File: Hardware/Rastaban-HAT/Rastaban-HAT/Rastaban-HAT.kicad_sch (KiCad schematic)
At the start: 65 parts, among them J1 1778780, J10 GPIO, J11 Conn_01x06_Male, J2 1778780, J3 1778780, J4 Screw_Terminal_01x02, J5 Jack-DC 12V+, J6 SM04B-SRSS-TB(LF)(SN), J7 Screw_Terminal_01x02, J8 Screw_Terminal_01x02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

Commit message: All files created with Jan
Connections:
- net at M1.1 (+): now also F1.2; no longer Q1.3 (D)
- net at M1.2 (-): now also Q1.3 (D); no longer F1.2
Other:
- moved on the sheet: M1
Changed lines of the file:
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@@
     (pin "2")
   )
-  (symbol (lib_id "Motor:Fan") (at 39.37 81.28 180) (unit 1)
-    (in_bom yes) (on_board yes)
-    (property "Reference" "M1" (id 0) (at 44.45 81.28 0))
-    (property "Value" "Fan" (id 1) (at 45.72 83.185 0)
-      (effects (font (size 1.27 1.27)) hide)
-    )
-    (property "Footprint" "Connector_PinHeader_2.54mm:PinHeader_1x02_P2.54mm_Vertical" (id 2) (at 39.37 81.534 0)
-      (effects (font (size 1.27 1.27)) hide)
-    )
-    (property "Datasheet" "~" (id 3) (at 39.37 81.534 0)
-      (effects (font (size 1.27 1.27)) hide)
-    )
-    (property "Purpose" "Cooling fan" (id 4) (at 48.26 84.455 0))
+  (symbol (lib_id "Motor:Fan") (at 39.37 83.82 0) (unit 1)
+    (in_bom yes) (on_board yes)
+    (property "Reference" "M1" (id 0) (at 34.29 83.82 0))
+    (property "Value" "Fan" (id 1) (at 33.02 81.915 0)
+      (effects (font (size 1.27 1.27)) hide)
+    )
+    (property "Footprint" "Connector_PinHeader_2.54mm:PinHeader_1x02_P2.54mm_Vertical" (id 2) (at 39.37 83.566 0)
+      (effects (font (size 1.27 1.27)) hide)
+    )
+    (property "Datasheet" "~" (id 3) (at 39.37 83.566 0)
+      (effects (font (size 1.27 1.27)) hide)
+    )
+    (property "Purpose" "Cooling fan" (id 4) (at 30.48 80.645 0))
     (pin "1")
     (pin "2")
@@
       (effects (font (size 1.27 1.27)) (justify right))
     )
-    (property "Value" "100uF 10V" (id 1) (at 38.735 38.735 0)
+    (property "Value" "100uF 10V" (id 1) (at 37.465 38.735 0)
       (effects (font (size 1.27 1.27)) (justify right))
     )
@@
       (effects (font (size 1.27 1.27)) (justify left))
     )
-    (property "Value" "10uF 10V" (id 1) (at 20.32 38.735 0)
-      (effects (font (size 1.27 1.27)) (justify left))
-    )
+    (property "Value" "10uF 10V" (id 1) (at 19.685 38.735 0)
+      (effects (font (size 1.27 1.27)) (justify left))
+    )

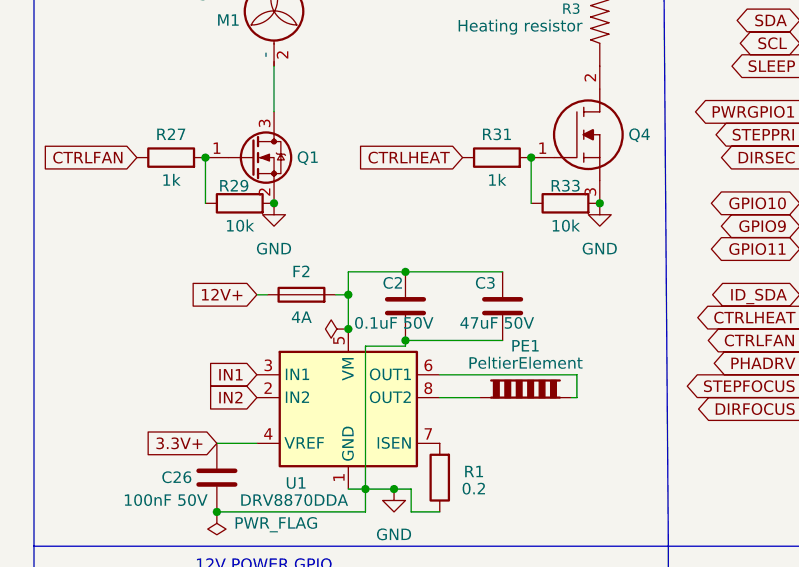
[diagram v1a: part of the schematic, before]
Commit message: enh pcb component layout
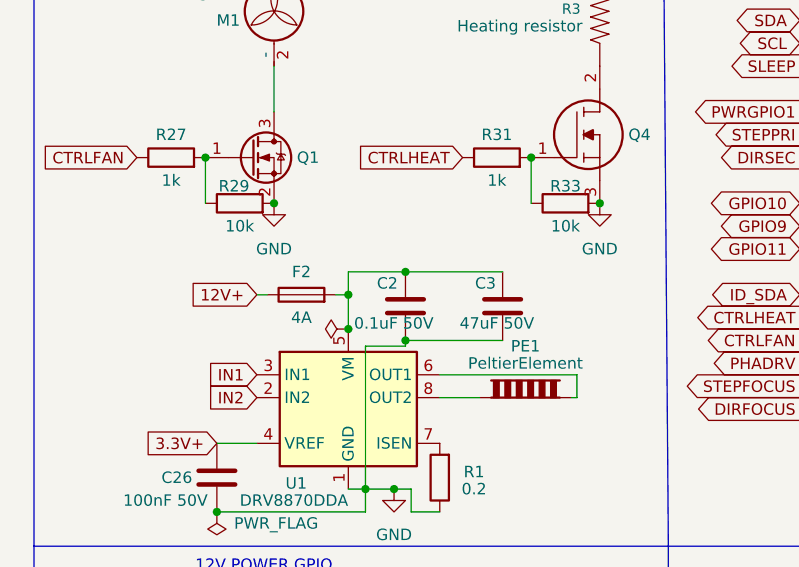
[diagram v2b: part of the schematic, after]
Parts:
- C1, C2, C20, C21, C25, C26, C3, C4: Purpose (none) -> decoupling
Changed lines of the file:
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@@
+      (effects (font (size 1.27 1.27)) hide)
+    )
+    (property "Purpose" "decoupling" (id 7) (at 64.77 115.57 0)
       (effects (font (size 1.27 1.27)) hide)
     )
@@
       (effects (font (size 1.27 1.27)) hide)
     )
+    (property "Purpose" "decoupling" (id 5) (at 198.12 71.755 0)
+      (effects (font (size 1.27 1.27)) hide)
+    )
     (pin "1")
     (pin "2")
@@
       (effects (font (size 1.27 1.27)) hide)
     )
+    (property "Purpose" "decoupling" (id 5) (at 196.85 117.475 0)
+      (effects (font (size 1.27 1.27)) hide)
+    )
     (pin "1")
     (pin "2")
@@
       (effects (font (size 1.27 1.27)) hide)
     )
+    (property "Purpose" "decoupling" (id 5) (at 233.045 88.265 0)
+      (effects (font (size 1.27 1.27)) hide)
+    )
     (pin "1")
     (pin "2")
@@
   (symbol (lib_id "Device:C") (at 53.975 115.57 180) (unit 1)
     (in_bom yes) (on_board yes)
-    (property "Reference" "C2" (id 0) (at 51.435 113.03 0)
+    (property "Reference" "C2" (id 0) (at 50.8 113.03 0)
       (effects (font (size 1.27 1.27)) (justify right))
     )
@@
     )
     (property "LCSC" "C28061" (id 4) (at 51.435 113.03 0)
+      (effects (font (size 1.27 1.27)) hide)
+    )
+    (property "Purpose" "decoupling" (id 5) (at 53.975 115.57 0)
       (effects (font (size 1.27 1.27)) hide)
     )
@@
       (effects (font (size 1.27 1.27)) hide)
     )
+    (property "Purpose" "decoupling" (id 5) (at 33.02 134.62 0)
+      (effects (font (size 1.27 1.27)) hide)
+    )
     (pin "1")
     (pin "2")
@@
     )
     (property "LCSC" "C3339" (id 6) (at 40.64 34.29 0)
+      (effects (font (size 1.27 1.27)) hide)
+    )
+    (property "Purpose" "decoupling" (id 7) (at 43.815 36.195 0)
       (effects (font (size 1.27 1.27)) hide)
     )
@@
       (effects (font (size 1.27 1.27)) hide)
     )
+    (property "Purpose" "decoupling" (id 7) (at 24.765 36.195 0)
+      (effects (font (size 1.27 1.27)) hide)
+    )

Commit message: almost finished grouping with older layout
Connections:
- net 3.3V+: now also R18.2; no longer R18.1
- net ID_SDA: now also R18.1; no longer R18.2
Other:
- moved on the sheet: R18
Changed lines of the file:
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@@
     (pin "2")
   )
-  (symbol (lib_id "Device:R_Small") (at 261.62 80.645 0) (unit 1)
+  (symbol (lib_id "Device:R_Small") (at 261.62 80.645 180) (unit 1)
     (in_bom yes) (on_board yes)
-    (property "Reference" "R18" (id 0) (at 256.54 79.375 0)
+    (property "Reference" "R18" (id 0) (at 266.7 81.915 0)
       (effects (font (size 1.27 1.27)) (justify left))
     )
-    (property "Value" "3.9k" (id 1) (at 255.905 81.915 0)
+    (property "Value" "3.9k" (id 1) (at 267.335 79.375 0)
       (effects (font (size 1.27 1.27)) (justify left))
     )

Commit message: general layout created pcb
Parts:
- J4, J7, J8, PE1: footprint TerminalBlock:TerminalBlock_Altech_AK300-2_P5.00mm -> TerminalBlock:TerminalBlock_bornier-2_P5.08mm
- R3: footprint Resistor_SMD:R_1206_3216Metric_Pad1.30x1.75mm_HandSolder -> Resistor_THT:R_Axial_DIN0309_L9.0mm_D3.2mm_P2.54mm_Vertical
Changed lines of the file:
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@@
       (effects (font (size 1.27 1.27)) (justify left) hide)
     )
-    (property "Footprint" "TerminalBlock:TerminalBlock_Altech_AK300-2_P5.00mm" (id 2) (at 45.72 167.005 0)
+    (property "Footprint" "TerminalBlock:TerminalBlock_bornier-2_P5.08mm" (id 2) (at 45.72 167.005 0)
       (effects (font (size 1.27 1.27)) hide)
     )
@@
       (effects (font (size 1.27 1.27)) (justify left) hide)
     )
-    (property "Footprint" "TerminalBlock:TerminalBlock_Altech_AK300-2_P5.00mm" (id 2) (at 178.435 24.765 0)
+    (property "Footprint" "TerminalBlock:TerminalBlock_bornier-2_P5.08mm" (id 2) (at 178.435 24.765 0)
       (effects (font (size 1.27 1.27)) hide)
     )
@@
     (property "Reference" "PE1" (id 0) (at 67.31 120.015 0))
     (property "Value" "PeltierElement" (id 1) (at 67.31 121.92 0))
-    (property "Footprint" "TerminalBlock:TerminalBlock_Altech_AK300-2_P5.00mm" (id 2) (at 67.31 127.508 0)
+    (property "Footprint" "TerminalBlock:TerminalBlock_bornier-2_P5.08mm" (id 2) (at 67.31 127.508 0)
       (effects (font (size 1.27 1.27)) hide)
     )
@@
       (effects (font (size 1.27 1.27)) (justify left) hide)
     )
-    (property "Footprint" "TerminalBlock:TerminalBlock_Altech_AK300-2_P5.00mm" (id 2) (at 80.645 167.005 0)
+    (property "Footprint" "TerminalBlock:TerminalBlock_bornier-2_P5.08mm" (id 2) (at 80.645 167.005 0)
       (effects (font (size 1.27 1.27)) hide)
     )
@@
       (effects (font (size 1 1)) hide)
     )
-    (property "Footprint" "Resistor_SMD:R_1206_3216Metric_Pad1.30x1.75mm_HandSolder" (id 2) (at 71.755 83.82 0)
+    (property "Footprint" "Resistor_THT:R_Axial_DIN0309_L9.0mm_D3.2mm_P2.54mm_Vertical" (id 2) (at 71.755 83.82 0)
       (effects (font (size 0.508 0.508)) hide)
     )
@@
     )
     (path "/5aac9ea9-4fe8-4ec4-82c6-ee5bf07b1349"
-      (reference "J4") (unit 1) (value "Screw_Terminal_01x02") (footprint "TerminalBlock:TerminalBlock_Altech_AK300-2_P5.00mm")
+      (reference "J4") (unit 1) (value "Screw_Terminal_01x02") (footprint "TerminalBlock:TerminalBlock_bornier-2_P5.08mm")
     )
     (path "/e220ca8d-f503-491c-aac3-31543f7f0722"
@@
     )
     (path "/00360c14-430e-4399-9d74-f52e2b63950e"
-      (reference "J7") (unit 1) (value "Screw_Terminal_01x02") (footprint "TerminalBlock:TerminalBlock_Altech_AK300-2_P5.00mm")
+      (reference "J7") (unit 1) (value "Screw_Terminal_01x02") (footprint "TerminalBlock:TerminalBlock_bornier-2_P5.08mm")
     )
     (path "/afd82313-5a87-47b5-9615-086f92b29aa8"
-      (reference "J8") (unit 1) (value "Screw_Terminal_01x02") (footprint "TerminalBlock:TerminalBlock_Altech_AK300-2_P5.00mm")
+      (reference "J8") (unit 1) (value "Screw_Terminal_01x02") (footprint "TerminalBlock:TerminalBlock_bornier-2_P5.08mm")
     )
     (path "/24bb24ca-3d2a-479f-b9a0-a9d8fbfb368d"
@@
     )
     (path "/a5a5959a-c687-4613-9524-73f0cec68824"
-      (reference "PE1") (unit 1) (value "PeltierElement") (footprint "TerminalBlock:TerminalBlock_Altech_AK300-2_P5.00mm")
+      (reference "PE1") (unit 1) (value "PeltierElement") (footprint "TerminalBlock:TerminalBlock_bornier-2_P5.08mm")
     )
     (path "/9a9094d0-3c31-47ba-80eb-52481aba703b"
@@
     )
     (path "/e2569925-ebf9-4052-bd02-8582502d3183"
-      (reference "R3") (unit 1) (value "1.20KOHM-0603-1_10W-1%") (footprint "Resistor_SMD:R_1206_3216Metric_Pad1.30x1.75mm_HandSolder")
+      (reference "R3") (unit 1) (value "1.20KOHM-0603-1_10W-1%") (footprint "Resistor_THT:R_Axial_DIN0309_L9.0mm_D3.2mm_P2.54mm_Vertical")
     )
     (path "/cb7fd693-d799-4afd-af49-3ab48484f6ca"

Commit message: changed capacitor footprints
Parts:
- C1, C5: footprint Capacitor_SMD:C_0805_2012Metric_Pad1.18x1.45mm_HandSolder -> Capacitor_SMD:CP_Elec_3x5.4
- C2, C3: footprint Capacitor_SMD:C_0805_2012Metric_Pad1.18x1.45mm_HandSolder -> Capacitor_SMD:CP_Elec_6.3x7.7
- C25, C26: footprint Capacitor_SMD:C_0805_2012Metric_Pad1.18x1.45mm_HandSolder -> Capacitor_SMD:CP_Elec_4x5.4
- C4: footprint Capacitor_SMD:C_0805_2012Metric_Pad1.18x1.45mm_HandSolder -> Capacitor_SMD:CP_Elec_8x10
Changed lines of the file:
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@@
     (property "Reference" "C3" (id 0) (at 62.865 113.03 0))
     (property "Value" "47uF 50V" (id 1) (at 64.135 117.475 0))
-    (property "Footprint" "Capacitor_SMD:C_0805_2012Metric_Pad1.18x1.45mm_HandSolder" (id 2) (at 63.8048 111.76 0)
+    (property "Footprint" "Capacitor_SMD:CP_Elec_6.3x7.7" (id 2) (at 63.8048 111.76 0)
       (effects (font (size 1.27 1.27)) hide)
     )
@@
       (effects (font (size 1.27 1.27)) (justify right))
     )
-    (property "Footprint" "Capacitor_SMD:C_0805_2012Metric_Pad1.18x1.45mm_HandSolder" (id 2) (at 233.045 88.265 0)
+    (property "Footprint" "Capacitor_SMD:CP_Elec_4x5.4" (id 2) (at 233.045 88.265 0)
       (effects (font (size 1.27 1.27)) hide)
     )
@@
       (effects (font (size 1.27 1.27)) (justify right))
     )
-    (property "Footprint" "Capacitor_SMD:C_0805_2012Metric_Pad1.18x1.45mm_HandSolder" (id 2) (at 53.0098 111.76 0)
+    (property "Footprint" "Capacitor_SMD:CP_Elec_6.3x7.7" (id 2) (at 53.0098 111.76 0)
       (effects (font (size 1.27 1.27)) hide)
     )
@@
     (property "Reference" "C26" (id 0) (at 28.575 134.62 0))
     (property "Value" "100nF 50V" (id 1) (at 27.305 137.16 0))
-    (property "Footprint" "Capacitor_SMD:C_0805_2012Metric_Pad1.18x1.45mm_HandSolder" (id 2) (at 32.0548 130.81 0)
+    (property "Footprint" "Capacitor_SMD:CP_Elec_4x5.4" (id 2) (at 32.0548 130.81 0)
       (effects (font (size 1.27 1.27)) hide)
     )
@@
       (effects (font (size 1.27 1.27)) (justify right))
     )
-    (property "Footprint" "Capacitor_SMD:C_0805_2012Metric_Pad1.18x1.45mm_HandSolder" (id 2) (at 42.8498 32.385 0)
+    (property "Footprint" "Capacitor_SMD:CP_Elec_8x10" (id 2) (at 42.8498 32.385 0)
       (effects (font (size 1.27 1.27)) hide)
     )
@@
       (effects (font (size 1.27 1.27)) (justify left))
     )
-    (property "Footprint" "Capacitor_SMD:C_0805_2012Metric_Pad1.18x1.45mm_HandSolder" (id 2) (at 228.2952 45.085 0)
+    (property "Footprint" "Capacitor_SMD:CP_Elec_3x5.4" (id 2) (at 228.2952 45.085 0)
       (effects (font (size 1.27 1.27)) hide)
     )
@@
       (effects (font (size 1.27 1.27)) (justify left))
     )
-    (property "Footprint" "Capacitor_SMD:C_0805_2012Metric_Pad1.18x1.45mm_HandSolder" (id 2) (at 25.7302 40.005 0)
+    (property "Footprint" "Capacitor_SMD:CP_Elec_3x5.4" (id 2) (at 25.7302 40.005 0)
       (effects (font (size 1.27 1.27)) hide)
     )
@@
     )
     (path "/f3fe5026-3ec3-4ef9-8ee4-ac53381f5d3c"
-      (reference "C1") (unit 1) (value "10uF 10V") (footprint "Capacitor_SMD:C_0805_2012Metric_Pad1.18x1.45mm_HandSolder")
+      (reference "C1") (unit 1) (value "10uF 10V") (footprint "Capacitor_SMD:CP_Elec_3x5.4")
     )
     (path "/6e705e76-606c-4ed6-ae7f-ed966b630818"
-      (reference "C2") (unit 1) (value "0.1uF 50V") (footprint "Capacitor_SMD:C_0805_2012Metric_Pad1.18x1.45mm_HandSolder")
+      (reference "C2") (unit 1) (value "0.1uF 50V") (footprint "Capacitor_SMD:CP_Elec_6.3x7.7")
     )
     (path "/023fab8f-e850-4f6d-bd01-c197d7adaf26"
-      (reference "C3") (unit 1) (value "47uF 50V") (footprint "Capacitor_SMD:C_0805_2012Metric_Pad1.18x1.45mm_HandSolder")
+      (reference "C3") (unit 1) (value "47uF 50V") (footprint "Capacitor_SMD:CP_Elec_6.3x7.7")
     )
     (path "/9f7db502-d21d-4e3f-97d2-a5c274cc55fe"
-      (reference "C4") (unit 1) (value "100uF 10V") (footprint "Capacitor_SMD:C_0805_2012Metric_Pad1.18x1.45mm_HandSolder")
+      (reference "C4") (unit 1) (value "100uF 10V") (footprint "Capacitor_SMD:CP_Elec_8x10")
     )
     (path "/bf4c234e-8821-4f3f-91ed-c4127b83d67d"
-      (reference "C5") (unit 1) (value "10uF 50V") (footprint "Capacitor_SMD:C_0805_2012Metric_Pad1.18x1.45mm_HandSolder")
+      (reference "C5") (unit 1) (value "10uF 50V") (footprint "Capacitor_SMD:CP_Elec_3x5.4")
     )
     (path "/6c4087b1-d585-4615-84b3-d395a8b5856d/69f29097-2575-4071-a5ad-9d8a6188f953"
-      (reference "C6") (unit 1) (value "10uF 25V") (footprint "Capacitor_SMD:C_0805_2012Metric_Pad1.18x1.45mm_HandSolder")
+      (reference "C6") (unit 1) (value "10uF 25V") (footprint "Capacitor_SMD:CP_Elec_3x5.4")
     )
     (path "/6c4087b1-d585-4615-84b3-d395a8b5856d/8b179e2f-dffe-4d2d-81d3-25372f70e7fb"
-      (reference "C7") (unit 1) (value "10uF 25V") (footprint "Capacitor_SMD:C_0805_2012Metric_Pad1.18x1.45mm_HandSolder")
+      (reference "C7") (unit 1) (value "10uF 25V") (footprint "Capacitor_SMD:CP_Elec_3x5.4")
     )
     (path "/6c4087b1-d585-4615-84b3-d395a8b5856d/f144db80-150c-4e1c-b463-12e5ce79f3e6"
-      (reference "C8") (unit 1) (value "100nF 50V") (footprint "Capacitor_SMD:C_0805_2012Metric_Pad1.18x1.45mm_HandSolder")
+      (reference "C8") (unit 1) (value "100nF 50V") (footprint "Capacitor_SMD:CP_Elec_4x5.4")
     )
     (path "/6c4087b1-d585-4615-84b3-d395a8b5856d/c3440438-0c3a-44cb-a190-31c82ffe96e5"
@@
     )
     (path "/6c4087b1-d585-4615-84b3-d395a8b5856d/62f9fb86-f705-4051-bd0e-ccfba8b3b0c0"
-      (reference "C11") (unit 1) (value "22uF 10V") (footprint "Capacitor_SMD:C_0805_2012Metric_Pad1.18x1.45mm_HandSolder")
+      (reference "C11") (unit 1) (value "22uF 10V") (footprint "Capacitor_SMD:CP_Elec_6.3x7.7")
     )
     (path "/6c4087b1-d585-4615-84b3-d395a8b5856d/cb026e0a-013a-4a17-87c5-4ed4f0628bfc"
-      (reference "C12") (unit 1) (value "22uF 10V") (footprint "Capacitor_SMD:C_0805_2012Metric_Pad1.18x1.45mm_HandSolder")
+      (reference "C12") (unit 1) (value "22uF 10V") (footprint "Capacitor_SMD:CP_Elec_6.3x7.7")
     )
     (path "/6c4087b1-d585-4615-84b3-d395a8b5856d/7514df18-9295-4870-9b15-d0d13f5e8b8b"
-      (reference "C13") (unit 1) (value "100nF 50V") (footprint "Capacitor_SMD:C_0805_2012Metric_Pad1.18x1.45mm_HandSolder")
+      (reference "C13") (unit 1) (value "100nF 50V") (footprint "Capacitor_SMD:CP_Elec_4x5.4")
     )
     (path "/7b03732c-6b0a-482e-b8e3-ced6ad7436b5/6a1389f5-af30-47b1-b0e6-d495f68a5530"
-      (reference "C14") (unit 1) (value "0.1uF 50V") (footprint "Capacitor_SMD:C_0805_2012Metric_Pad1.18x1.45mm_HandSolder")
+      (reference "C14") (unit 1) (value "0.1uF 50V") (footprint "Capacitor_SMD:CP_Elec_6.3x7.7")
     )
     (path "/7b03732c-6b0a-482e-b8e3-ced6ad7436b5/45cf8dc3-5f81-4af3-b0d1-8379078362f4"
-      (reference "C15") (unit 1) (value "0.1uF 50V") (footprint "Capacitor_SMD:C_0805_2012Metric_Pad1.18x1.45mm_HandSolder")
+      (reference "C15") (unit 1) (value "0.1uF 50V") (footprint "Capacitor_SMD:CP_Elec_6.3x7.7")
     )
     (path "/509754cd-dbf1-46e6-965c-38d41c0b6924/b391f05e-9d79-4808-8c88-d0da93b38ae2"
-      (reference "C16") (unit 1) (value "100uF 35V") (footprint "Capacitor_THT:C_Radial_D6.3mm_H5.0mm_P2.50mm")
+      (reference "C16") (unit 1) (value "100uF 35V") (footprint "Capacitor_SMD:CP_Elec_8x10")
     )
     (path "/509754cd-dbf1-46e6-965c-38d41c0b6924/e00c426b-f72a-4212-94e0-d9ce7621402d"
-      (reference "C17") (unit 1) (value "100uF 35V") (footprint "Capacitor_THT:C_Radial_D6.3mm_H11.0mm_P2.50mm")
+      (reference "C17") (unit 1) (value "100uF 35V") (footprint "Capacitor_SMD:CP_Elec_8x10")
     )
     (path "/7b03732c-6b0a-482e-b8e3-ced6ad7436b5/6a92e50c-ed6c-499b-95da-e3221c59e174"
-      (reference "C18") (unit 1) (value "100nF 35V") (footprint "Capacitor_THT:C_Radial_D6.3mm_H11.0mm_P2.50mm")
+      (reference "C18") (unit 1) (value "100uF 35V") (footprint "Capacitor_SMD:CP_Elec_8x10")
     )
     (path "/7b03732c-6b0a-482e-b8e3-ced6ad7436b5/e5d64b5c-b610-4e2e-9355-8b38ef775df4"
-      (reference "C19") (unit 1) (value "10uF 10V") (footprint "Capacitor_THT:C_Radial_D6.3mm_H11.0mm_P2.50mm")
+      (reference "C19") (unit 1) (value "10uF 10V") (footprint "Capacitor_SMD:CP_Elec_3x5.4")
     )
     (path "/417244c7-860c-431e-83b5-557b7eb46186"
@@
     )
     (path "/509754cd-dbf1-46e6-965c-38d41c0b6924/ea895115-43dd-412e-a12c-5a4bbf8914e0"
-      (reference "C22") (unit 1) (value "100nF 6.3V") (footprint "Capacitor_SMD:C_0805_2012Metric_Pad1.18x1.45mm_HandSolder")
+      (reference "C22") (unit 1) (value "100nF 6.3V") (footprint "Capacitor_SMD:CP_Elec_4x5.4")
     )
     (path "/509754cd-dbf1-46e6-965c-38d41c0b6924/398454fc-117f-46f9-a536-a0824937f2c4"
-      (reference "C23") (unit 1) (value "100nF 6.3V") (footprint "Capacitor_SMD:C_0805_2012Metric_Pad1.18x1.45mm_HandSolder")
+      (reference "C23") (unit 1) (value "100nF 6.3V") (footprint "Capacitor_SMD:CP_Elec_4x5.4")
     )
     (path "/7b03732c-6b0a-482e-b8e3-ced6ad7436b5/d82a4c9c-4d57-45b3-be3e-d497c1cc4ec7"
-      (reference "C24") (unit 1) (value "100nF 6.3V") (footprint "Capacitor_SMD:C_0805_2012Metric_Pad1.18x1.45mm_HandSolder")
+      (reference "C24") (unit 1) (value "100nF 6.3V") (footprint "Capacitor_SMD:CP_Elec_4x5.4")
     )
     (path "/6d1772b3-b434-4c39-820a-75c27b63c8e3"
-      (reference "C25") (unit 1) (value "100nF 50V") (footprint "Capacitor_SMD:C_0805_2012Metric_Pad1.18x1.45mm_HandSolder")
+      (reference "C25") (unit 1) (value "100nF 50V") (footprint "Capacitor_SMD:CP_Elec_4x5.4")
     )
     (path "/6fd24ba3-02a6-4dad-b537-cd582941af2f"
-      (reference "C26") (unit 1) (value "100nF 50V") (footprint "Capacitor_SMD:C_0805_2012Metric_Pad1.18x1.45mm_HandSolder")
+      (reference "C26") (unit 1) (value "100nF 50V") (footprint "Capacitor_SMD:CP_Elec_4x5.4")
     )
     (path "/ccd151f8-b6e8-466d-9216-2c2b207285eb"

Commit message: added leds for all temperature, mic led and power gpio
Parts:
- added D10, D11, D12, D13, D7, D8, D9: LED, LED_SMD:LED_0805_2012Metric_Pad1.15x1.40mm_HandSolder, symbol Device:LED
- added R15, R16, R17, R26, R35, R36, R37: 330, Resistor_SMD:R_0805_2012Metric_Pad1.20x1.40mm_HandSolder, symbol Device:R
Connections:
- net CTRLFAN: now also D9.2 (A)
- net CTRLHEAT: now also D10.2 (A)
- net CTRLLED: now also D11.2 (A)
- net GND: now also R15.2, R16.2, R17.2, R26.2, R35.2, R36.2, R37.2
- net IN1: now also D7.2 (A)
- net IN2: now also D8.2 (A)
- net PWRGPIO1: now also D12.2 (A)
- net PWRGPIO2: now also D13.2 (A)
- new net: D10.1 (K), R26.1
- new net: D11.1 (K), R35.1
- new net: D12.1 (K), R36.1
- new net: D13.1 (K), R37.1
- new net: D9.1 (K), R17.1
- new net: D7.1 (K), R15.1
- new net: D8.1 (K), R16.1
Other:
- note added: "LED signals"

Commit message: added testpoints
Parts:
- added TP? (x7): TestPoint, TestPoint:TestPoint_THTPad_2.0x2.0mm_Drill1.0mm, symbol Connector:TestPoint
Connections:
- net CTRLFAN: now also TP?.1
- net CTRLHEAT: now also TP?.1
- net CTRLLED: now also TP?.1
- net IN1: now also TP?.1
- net IN2: now also TP?.1
- net PWRGPIO1: now also TP?.1
- net PWRGPIO2: now also TP?.1
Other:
- moved on the sheet: D10, D11, D12, D13, D7, D8, D9, R15, R16, R17, R26, R35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

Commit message: Removed LEDS
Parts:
- removed D10, D11, D12, D13, D7, D8, D9: LED, LED_SMD:LED_0805_2012Metric_Pad1.15x1.40mm_HandSolder, symbol Device:LED
- removed R15, R16, R17, R26, R35, R36, R37: 330, Resistor_SMD:R_0805_2012Metric_Pad1.20x1.40mm_HandSolder, symbol Device:R
- gave numbers to parts that had none: 7
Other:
- note removed: "LED signals"
- moved on the sheet: TP10, TP11, TP2, TP5, TP6, TP8, TP9
